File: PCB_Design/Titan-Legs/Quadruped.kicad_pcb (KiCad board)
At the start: 4 copper layers, 55.5 x 55.5 mm, 85 parts, among them IC1 TPS54260DGQR, IC2 CP2102, IC3 DRV8323RSRGZT, J1 TYPE-C-31-M-12, J2 691214110003, P1 282837-2, P2 282837-2, Q1 BSC031N06NS3GATMA1, Q2 BSC031N06NS3GATMA1, Q3 BSC031N06NS3GATMA1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

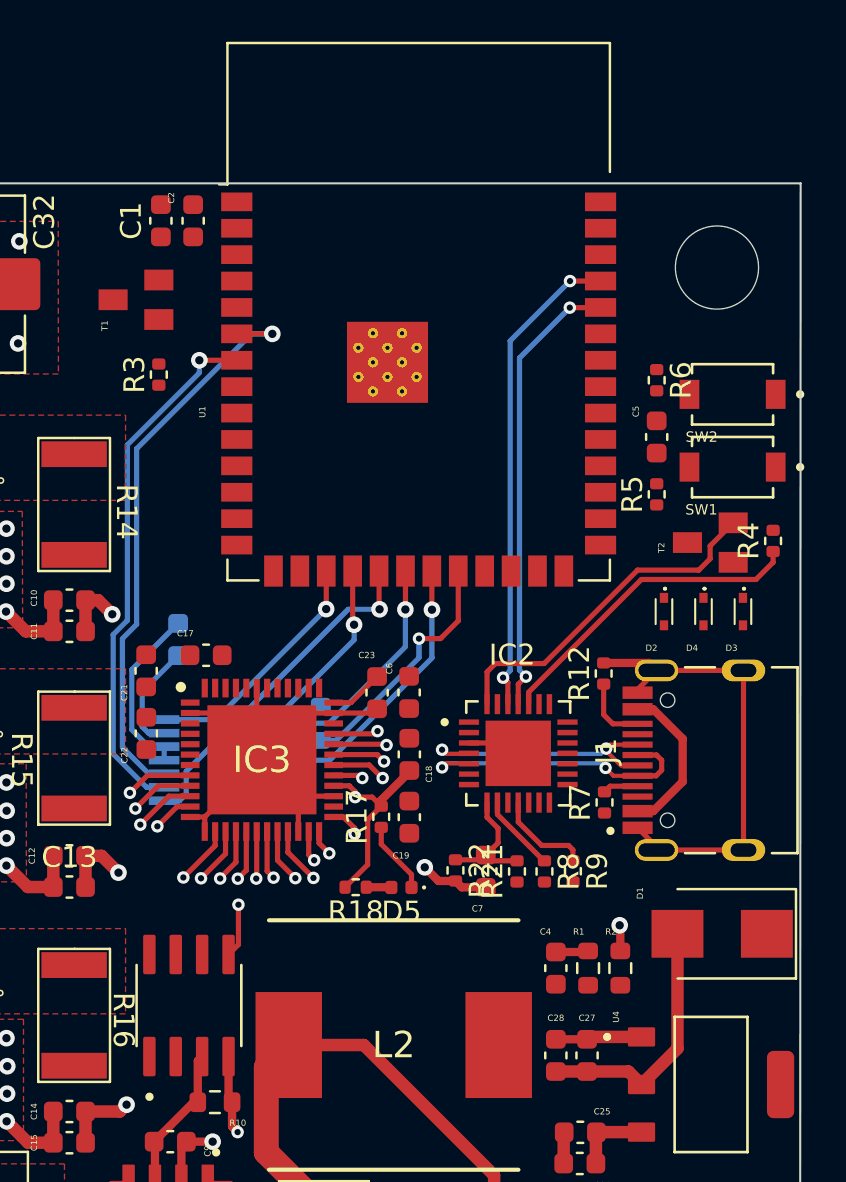
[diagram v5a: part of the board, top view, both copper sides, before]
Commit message: Added Complete ESP32 net traces
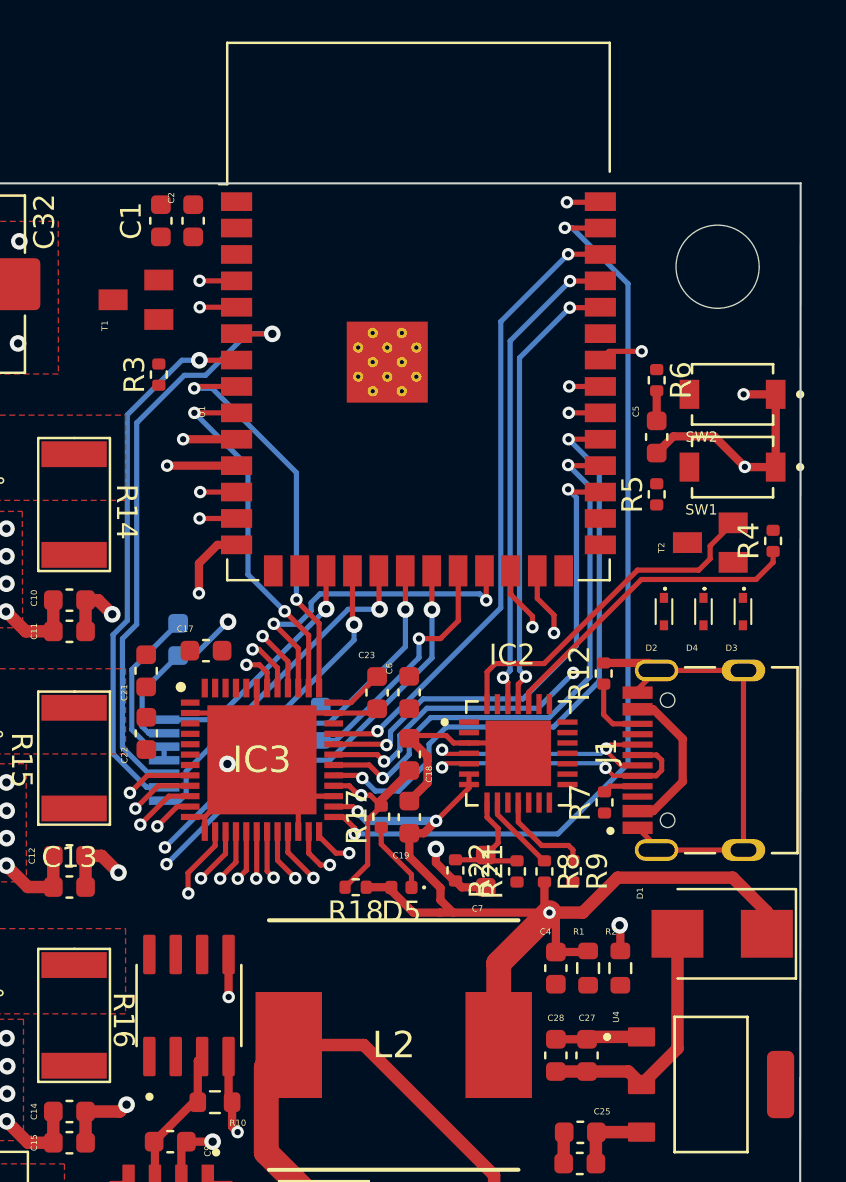
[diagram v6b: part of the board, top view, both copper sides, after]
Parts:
- moved C17 0.22 mm to (55.7, 97.8)
- moved H2 0.05 mm to (80.3, 79.4)
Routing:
- net 3V3_IN: track 18.6 -> 65.0 mm, vias 0 -> 3
- net /IO1: track 1.51 -> 45.0 mm, vias 1 -> 2
- net /IO17: track 2.27 -> 45.6 mm, vias 1 -> 2
- net /IO4: track 0.00 -> 41.1 mm, vias 0 -> 2
- net /IO18: track 2.19 -> 42.6 mm, vias 1 -> 2
- net /IO5: track 0.00 -> 38.6 mm, vias 0 -> 2
- net /IO41: track 0.00 -> 32.8 mm, vias 0 -> 2
- net /IO20: track 3.82 -> 35.1 mm, vias 1 -> 2
- net /IO2: track 2.16 -> 30.5 mm, vias 1 -> 2
- net /IO38: track 1.43 -> 29.5 mm, vias 1 -> 2
- net /IO39: track 0.00 -> 26.6 mm, vias 0 -> 2
- net GND: track 91.5 -> 117.2 mm, vias 24 -> 29
- net /IO8: track 1.25 -> 26.9 mm, vias 1 -> 2
- net /IO19: track 1.49 -> 27.1 mm, vias 1 -> 2
- net /IO40: track 0.00 -> 25.3 mm, vias 0 -> 2
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
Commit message: Added DRV8323RS Traces and some minor changes
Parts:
- moved R1 14.9 mm to (73.3, 127.9)
- moved R2 14.9 mm to (74.9, 127.9)
- moved C3 4.66 mm to (73.7, 121.4)
- moved C30 4.66 mm to (73.7, 124.4)
- moved R24 4.66 mm to (73.7, 122.9)
- moved C26 3.40 mm to (73.6, 119.1)
- moved C25 3.40 mm to (73.6, 117.6)
- moved C27 2.52 mm to (74.4, 114.8)
- moved C28 2.52 mm to (72.9, 114.8)
- moved C4 2.07 mm to (74.2, 111.8), turned to 0 degrees
- moved C29 1.12 mm to (64.0, 126.0)
- moved R23 1.12 mm to (64.0, 129.0)
- moved D_Zener1 0.54 mm to (60.8, 126.9)
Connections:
- IC1 pad 12: (no net) -> GND
- IC1 pad 13: (no net) -> GND
- IC1 pad 14: (no net) -> GND
- IC1 pad 15: (no net) -> GND
- IC1 pad 16: (no net) -> GND
- R13 pad 1: /CAN_BUS_IC/IO38 -> /IO35
- U1 pad 28: unconnected-(U1-Pad28) -> /IO35
- U1 pad 41: (no net) -> GND
- U3 pad 8: /CAN_BUS_IC/IO38 -> /IO35
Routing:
- net /IO35: track 0.00 -> 49.8 mm, vias 0 -> 3
- net /DRV8323/MOTOR_C: track 2.35 -> 46.0 mm
- net GND: track 117.2 -> 149.4 mm, vias 29 -> 45
- net /DRV8323/MOTOR_B: track 2.57 -> 32.8 mm
- net VM: track 12.5 -> 41.3 mm, vias 43 -> 44
- net /DRV8323/GHC: track 2.27 -> 27.6 mm, vias 1 -> 2
- net /DRV8323/MOTOR_A: track 3.09 -> 27.1 mm
- net /DRV8323/GHB: track 2.44 -> 24.1 mm, vias 1 -> 2
- net /DRV8323/GLB: track 2.74 -> 22.0 mm, vias 1 -> 2
- net /DRV8323/GHA: track 3.25 -> 21.8 mm, vias 1 -> 2
- net /DRV8323/SPB: track 3.52 -> 19.2 mm, vias 1 -> 2
- net /D-: track 14.1 -> 24.2 mm, vias 2 -> 4
- net /BOOT: track 0.00 -> 9.81 mm
- net /EN: track 1.45 -> 10.7 mm
- net /D+: track 13.0 -> 21.6 mm, vias 2 -> 4
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
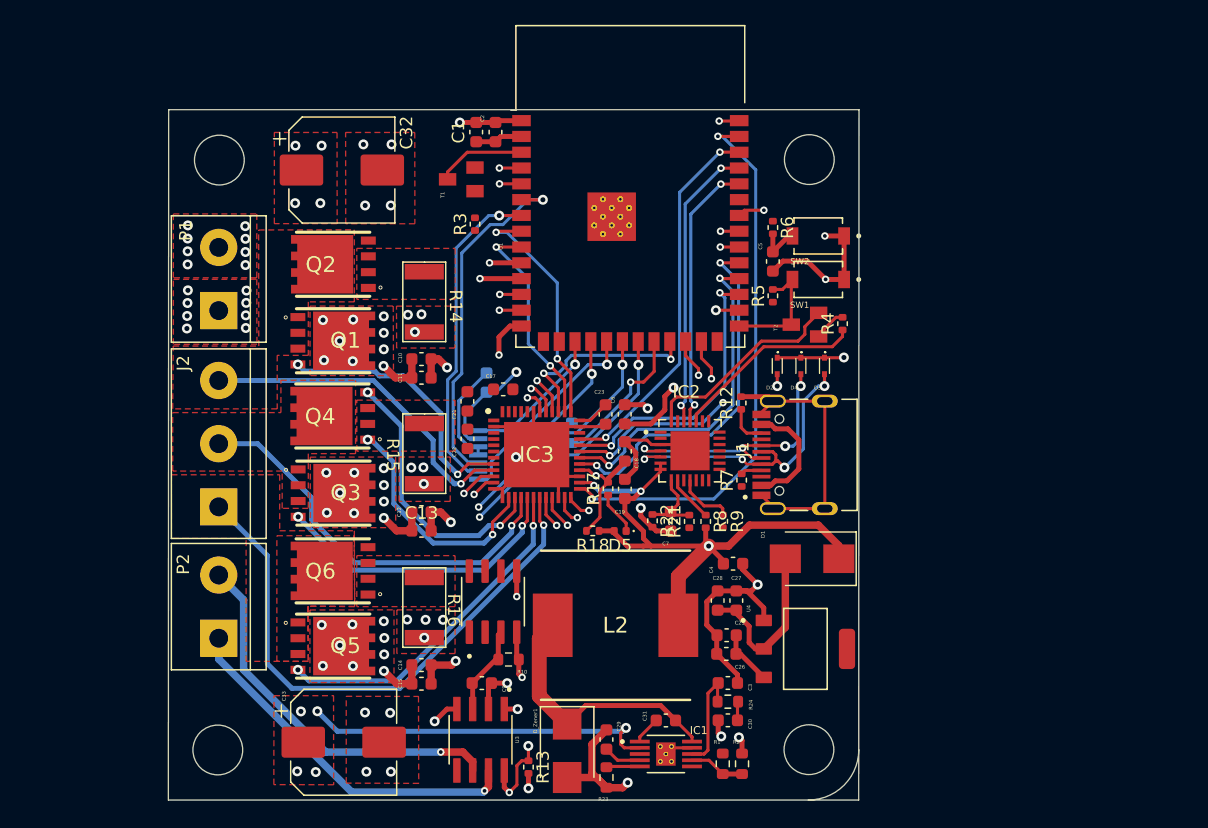
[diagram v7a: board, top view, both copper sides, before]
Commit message: Completed PCB Routing
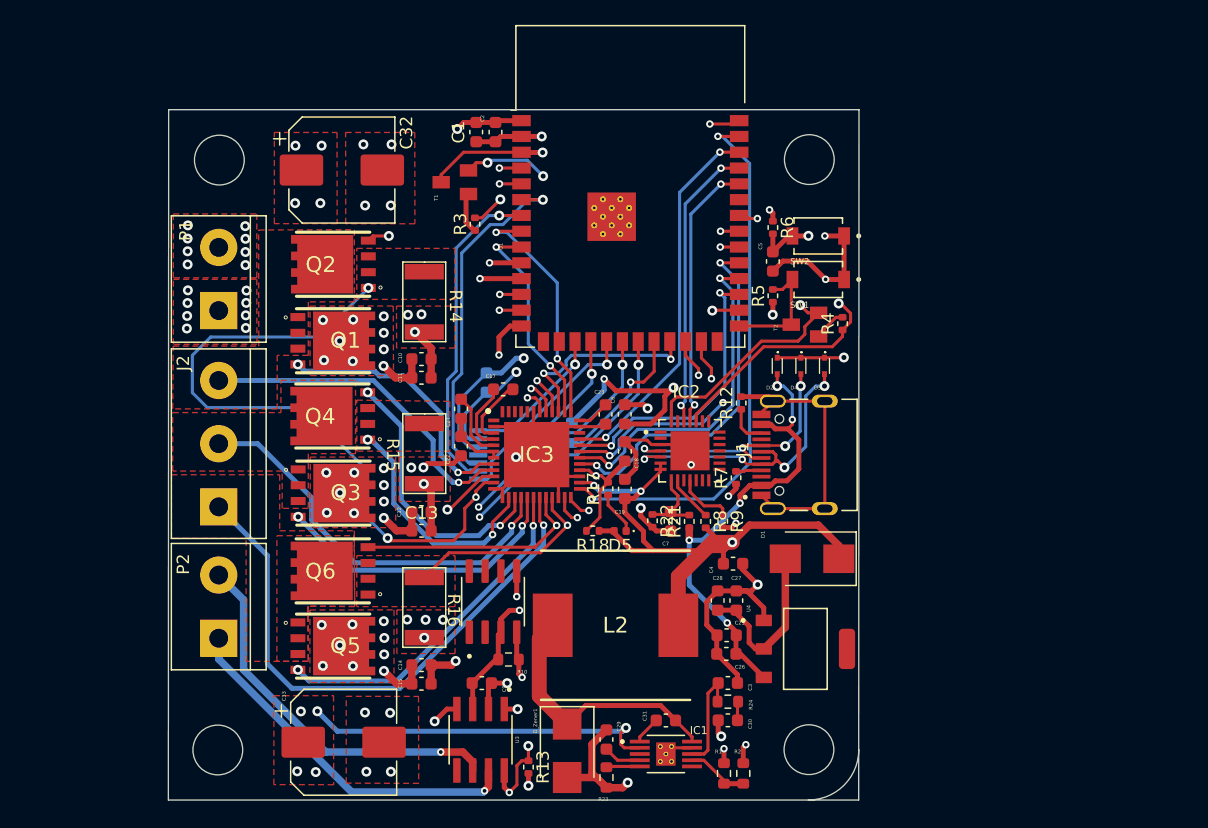
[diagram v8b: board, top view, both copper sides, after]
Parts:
- moved C21 0.79 mm to (52.3, 99.4)
- moved C22 0.79 mm to (52.3, 102.4)
- moved R1 0.78 mm to (73.4, 128.7)
- moved R2 0.78 mm to (75.0, 128.7)
- moved T1 0.57 mm to (51.8, 81.2)
- moved R7 0.49 mm to (74.4, 104.9)
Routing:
- net /DRV8323/SPA: track 1.97 -> 54.0 mm, vias 1 -> 3
- net /RTS: track 15.4 -> 54.8 mm, vias 0 -> 3
- net /DTR: track 16.7 -> 52.1 mm, vias 0 -> 2
- net /DRV8323/GLA: track 2.97 -> 31.1 mm, vias 1 -> 2
- net /EN: track 10.7 -> 38.5 mm, vias 0 -> 2
- net 3V3_IN: track 72.9 -> 98.7 mm, vias 4 -> 11
- net VBUS: track 14.9 -> 37.5 mm, vias 1 -> 5
- net /DRV8323/GLC: track 2.60 -> 18.5 mm
- net /DRV8323/SPC: track 2.74 -> 16.0 mm
- net GND: track 149.4 -> 158.2 mm, vias 45 -> 46
- net /DRV8323/CPH: track 0.00 -> 5.66 mm
- net /DRV8323/CPL: track 0.00 -> 5.51 mm
- net /DRV8323/VCP: track 0.00 -> 5.39 mm
- net VM: track 41.3 -> 46.3 mm
- net Net-(R3-Pad1): track 0.00 -> 3.34 mm
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- added copper zone on In1.Cu, net 3V3_IN
- added copper zone on In2.Cu, net GND
